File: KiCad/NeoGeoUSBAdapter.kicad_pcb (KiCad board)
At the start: 2 copper layers, 48.3 x 43.2 mm, 3 parts

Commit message: Small improvements in PCB
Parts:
- moved CONN_P2 70.7 mm to (174.5, 91.3)
- moved ? 70.7 mm to (160.7, 74.9)
- moved CONN_P1 70.7 mm to (146.9, 71.9)
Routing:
- net (no net): track 296.1 -> 316.6 mm

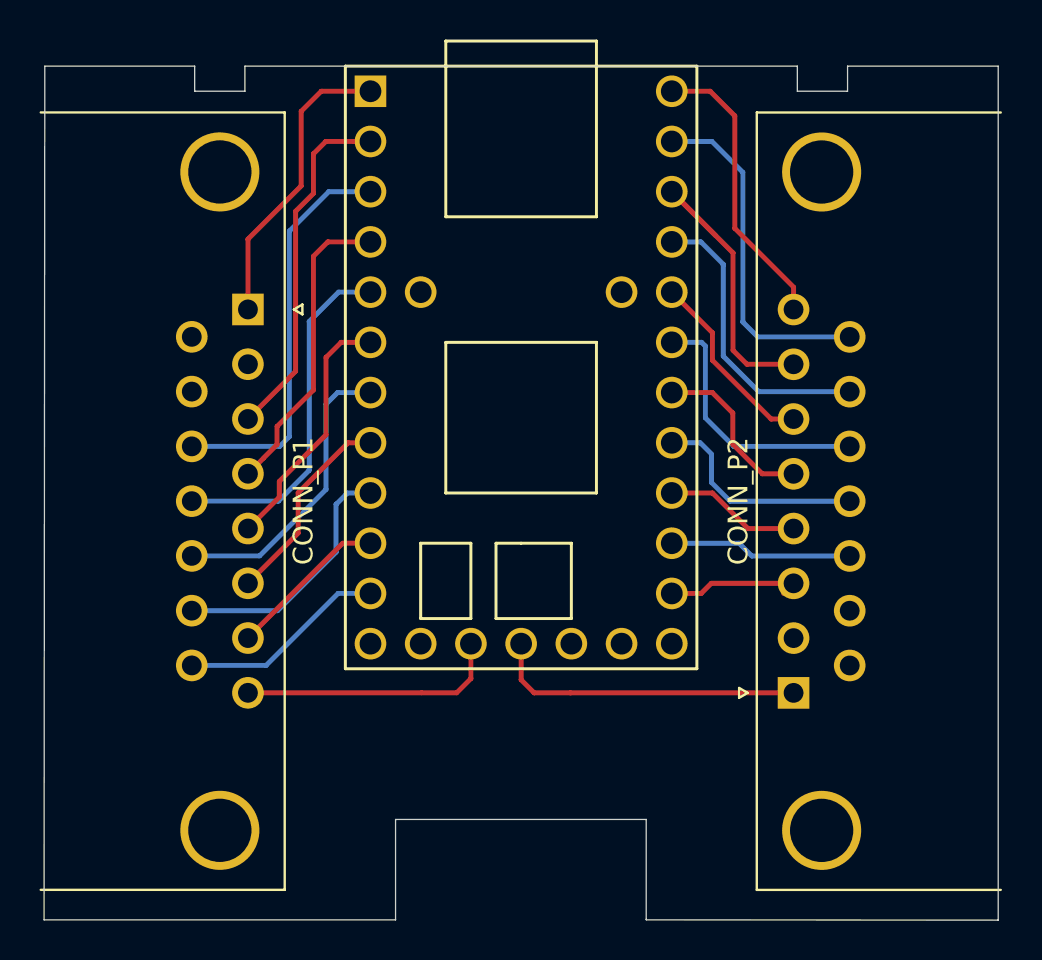
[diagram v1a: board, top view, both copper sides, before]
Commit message: PCB : add GND network and ground plane
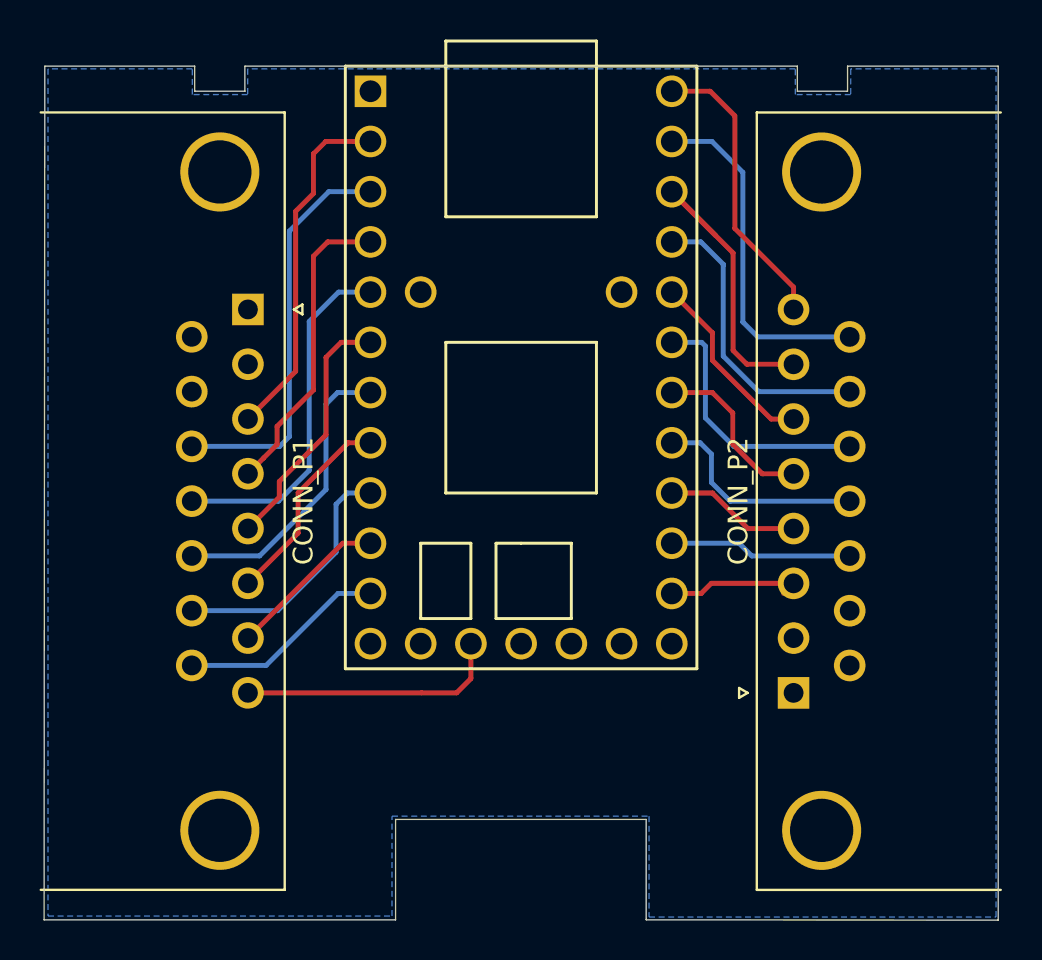
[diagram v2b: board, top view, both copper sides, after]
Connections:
- ? pad 1: (no net) -> GND
- ? pad 15: (no net) -> GND
- CONN_P1 pad 1: (no net) -> GND
- CONN_P2 pad 1: (no net) -> GND
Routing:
- net (no net): track 316.6 -> 285.7 mm
- added copper zone on B.Cu, net GND
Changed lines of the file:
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@@
     (thickness 1.6)
     (drawings 17)
-    (tracks 115)
+    (tracks 106)
     (zones 0)
     (modules 3)
-    (nets 1)
+    (nets 2)
   )
   (page A4)
@@
   )
   (net 0 "")
+  (net 1 GND)
   (net_class Default "This is the default net class."
     (clearance 0.2)
@@
     (uvia_dia 0.3)
     (uvia_drill 0.1)
+    (add_net GND)
   )
   (module Connectors_DSUB:DSUB-15_Male_Horizontal_Pitch2.77x2.84mm_EdgePinOffset7.70mm_Housed_MountingHolesOffset9.12mm (layer F.Cu)
@@
     (pad 3 thru_hole circle (at 5.54 0 90) (size 1.6 1.6) (drill 1) (layers *.Cu *.Mask))
     (pad 2 thru_hole circle (at 2.77 0 90) (size 1.6 1.6) (drill 1) (layers *.Cu *.Mask))
-    (pad 1 thru_hole rect (at 0 0 90) (size 1.6 1.6) (drill 1) (layers *.Cu *.Mask))
+    (pad 1 thru_hole rect (at 0 0 90) (size 1.6 1.6) (drill 1) (layers *.Cu *.Mask)
+      (net 1 GND))
     (model ${KISYS3DMOD}/Connectors_DSub.3dshapes/DSUB-15_Male_Horizontal_Pitch2.77x2.84mm_EdgePinOffset7.70mm_Housed_MountingHolesOffset9.12mm.wrl
       (at (xyz 0 0 0))
@@
     (fp_line (start 15.24 8.89) (end -15.24 8.89) (layer F.SilkS) (width 0.15))
     (fp_line (start -15.24 8.89) (end -15.24 -8.89) (layer F.SilkS) (width 0.15))
-    (pad 15 thru_hole circle (at 13.97 0 270) (size 1.6 1.6) (drill 1.1) (layers *.Cu *.Mask F.SilkS))
-    (pad 1 thru_hole rect (at -13.97 7.62 270) (size 1.6 1.6) (drill 1.1) (layers *.Cu *.Mask F.SilkS))
+    (pad 15 thru_hole circle (at 13.97 0 270) (size 1.6 1.6) (drill 1.1) (layers *.Cu *.Mask F.SilkS)
+      (net 1 GND))
+    (pad 1 thru_hole rect (at -13.97 7.62 270) (size 1.6 1.6) (drill 1.1) (layers *.Cu *.Mask F.SilkS)
+      (net 1 GND))
     (pad 2 thru_hole circle (at -11.43 7.62 270) (size 1.6 1.6) (drill 1.1) (layers *.Cu *.Mask F.SilkS))
     (pad 3 thru_hole circle (at -8.89 7.62 270) (size 1.6 1.6) (drill 1.1) (layers *.Cu *.Mask F.SilkS))
@@
       (effects (font (size 1 1) (thickness 0.15)))
     )
-    (pad 1 thru_hole rect (at 0 0 270) (size 1.6 1.6) (drill 1) (layers *.Cu *.Mask))
+    (pad 1 thru_hole rect (at 0 0 270) (size 1.6 1.6) (drill 1) (layers *.Cu *.Mask)
+      (net 1 GND))
     (pad 2 thru_hole circle (at 2.77 0 270) (size 1.6 1.6) (drill 1) (layers *.Cu *.Mask))
     (pad 3 thru_hole circle (at 5.54 0 270) (size 1.6 1.6) (drill 1) (layers *.Cu *.Mask))
@@
   (segment (start 152.2504 63.4238) (end 153.0604 63.4238) (width 0.25) (layer F.Cu) (net 0))
   (segment (start 168.7604 85.8238) (end 168.3004 86.2838) (width 0.25) (layer F.Cu) (net 0))
-  (segment (start 146.8628 71.9201) (end 146.8628 68.3641) (width 0.25) (layer F.Cu) (net 0))
-  (segment (start 146.8628 68.3641) (end 149.5552 65.6717) (width 0.25) (layer F.Cu) (net 0))
-  (segment (start 149.5552 65.6717) (end 149.5552 61.8998) (width 0.25) (layer F.Cu) (net 0))
-  (segment (start 150.5712 60.8838) (end 153.0604 60.8838) (width 0.25) (layer F.Cu) (net 0))
-  (segment (start 149.5552 61.8998) (end 150.5712 60.8838) (width 0.25) (layer F.Cu) (net 0))
   (segment (start 150.7998 63.4238) (end 153.0604 63.4238) (width 0.25) (layer F.Cu) (net 0))
   (segment (start 150.1775 64.0461) (end 150.7998 63.4238) (width 0.25) (layer F.Cu) (net 0))
@@
   (segment (start 146.8628 88.5401) (end 151.6591 83.7438) (width 0.25) (layer F.Cu) (net 0))
   (segment (start 146.8628 91.3101) (end 155.6541 91.3101) (width 0.25) (layer F.Cu) (net 0))
-  (segment (start 174.4599 91.313) (end 163.1696 91.313) (width 0.25) (layer F.Cu) (net 0))
   (segment (start 173.9491 86.2838) (end 174.4599 85.773) (width 0.25) (layer F.Cu) (net 0))
   (segment (start 168.3004 71.3035) (end 168.3004 71.0438) (width 0.25) (layer F.Cu) (net 0))
@@
   (segment (start 157.4194 91.3101) (end 155.6541 91.3101) (width 0.25) (layer F.Cu) (net 0))
   (segment (start 158.1404 90.5891) (end 157.4194 91.3101) (width 0.25) (layer F.Cu) (net 0))
-  (segment (start 160.6804 88.8238) (end 160.6804 90.6526) (width 0.25) (layer F.Cu) (net 0))
-  (segment (start 161.3408 91.313) (end 163.1696 91.313) (width 0.25) (layer F.Cu) (net 0))
-  (segment (start 160.6804 90.6526) (end 161.3408 91.313) (width 0.25) (layer F.Cu) (net 0))
   (segment (start 168.3004 81.2038) (end 170.3578 81.2038) (width 0.25) (layer F.Cu) (net 0))
   (segment (start 170.3578 81.2038) (end 172.1612 83.0072) (width 0.25) (layer F.Cu) (net 0))
@@
   (segment (start 151.4221 86.2838) (end 147.7808 89.9251) (width 0.25) (layer B.Cu) (net 0))
   (segment (start 153.0604 86.2838) (end 151.4221 86.2838) (width 0.25) (layer B.Cu) (net 0))
+  (zone (net 1) (net_name GND) (layer B.Cu) (hatch edge 0.508)
+    (connect_pads (clearance 0.508))
+    (min_thickness 0.254)
+    (fill yes (arc_segments 32) (thermal_gap 0.508) (thermal_bridge_width 0.508))
+    (polygon
+      (pts
+        (xy 184.7 59.75) (xy 177.35 59.75) (xy 177.35 61.05) (xy 174.55 61.05) (xy 174.55 59.75)
+        (xy 146.85 59.75) (xy 146.85 61.05) (xy 144.05 61.05) (xy 144.05 59.75) (xy 136.75 59.75)
+        (xy 136.75 102.6) (xy 154.15 102.6) (xy 154.15 97.55) (xy 167.15 97.55) (xy 167.15 102.65)
+        (xy 184.7 102.65)
+      )
+    )
+  )
 )

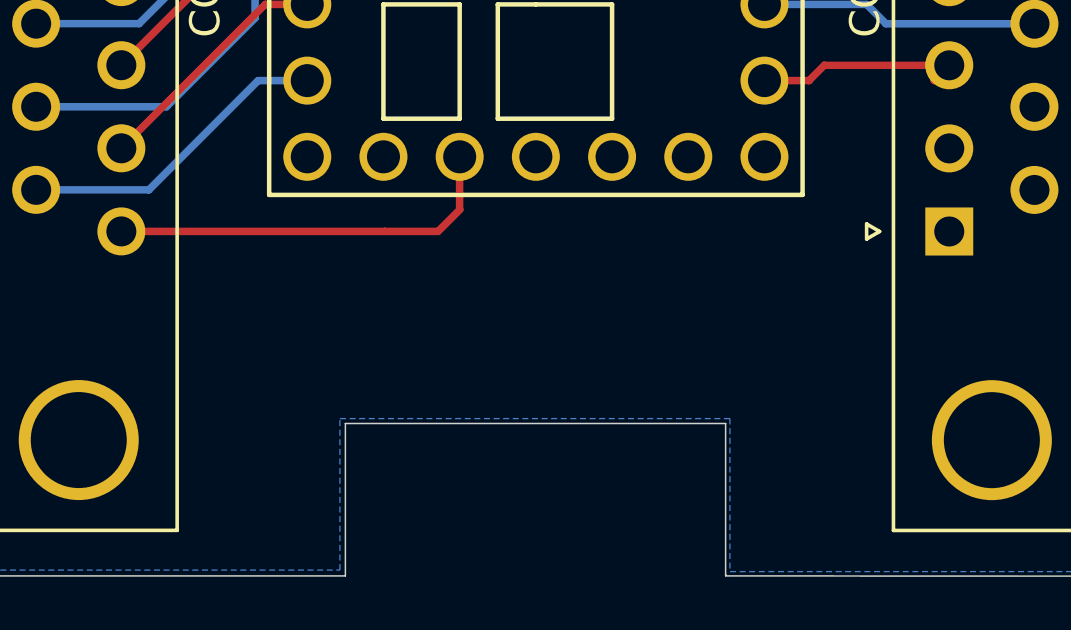
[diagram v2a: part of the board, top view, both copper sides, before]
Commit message: PCB : add Front and Back Silk Layers
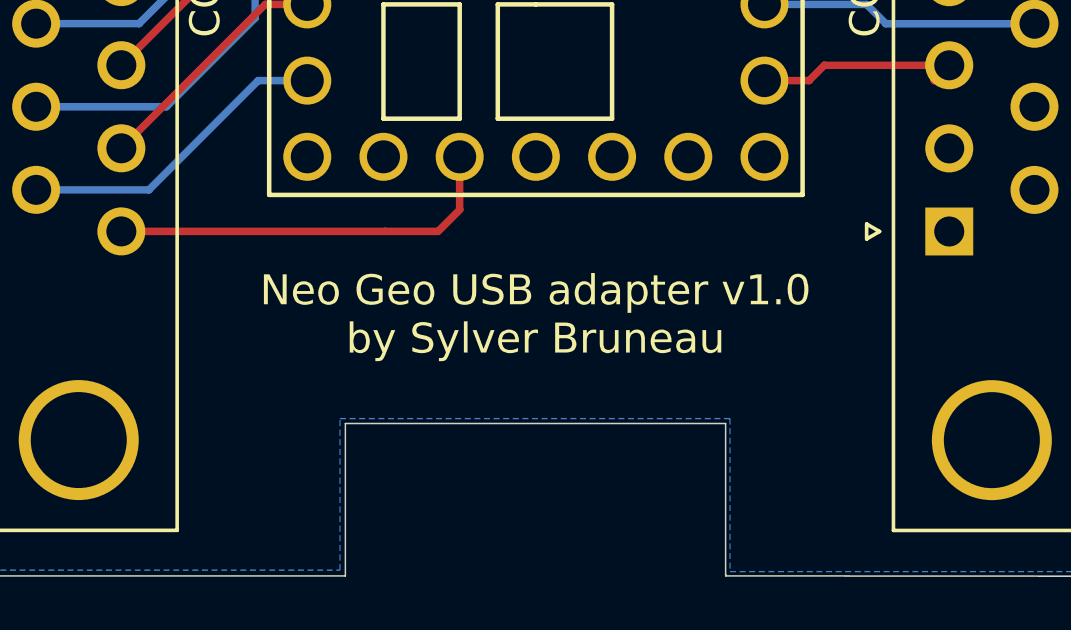
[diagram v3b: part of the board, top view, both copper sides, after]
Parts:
- added G***: LOGO, NeoGeo:NeoGeo, F.Cu at (160.7, 78.9)
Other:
- board text added: "By Sylver Bruneau"
- board text added: "Neo Geo USB adapter v1.0 by Sylver Bruneau"
- board text added: "v1.0"
